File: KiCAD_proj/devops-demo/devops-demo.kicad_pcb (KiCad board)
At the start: 2 copper layers, 8 parts, among them J1 Conn_PinHeader_FTDI_1x06_P2.5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, SW1 SWITCH_JS102011JCQN, U1 ESP32-WROOM-32, U2 AMS1117-3.3

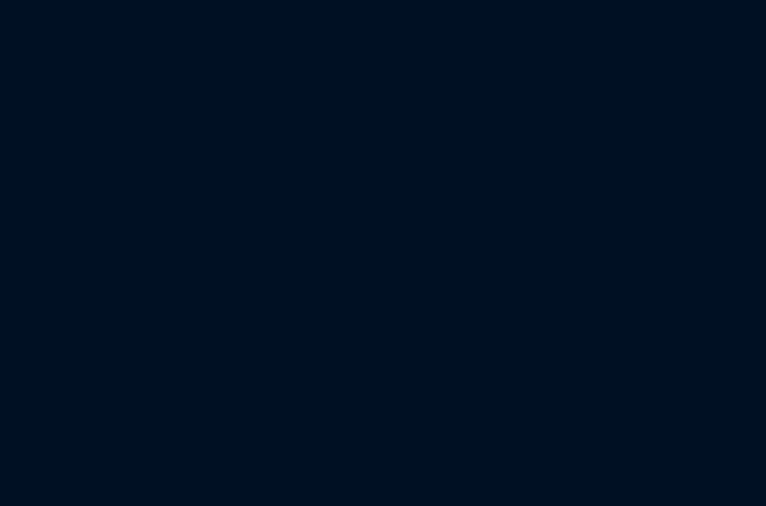
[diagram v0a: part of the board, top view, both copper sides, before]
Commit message: Added PWR and RESET circuits
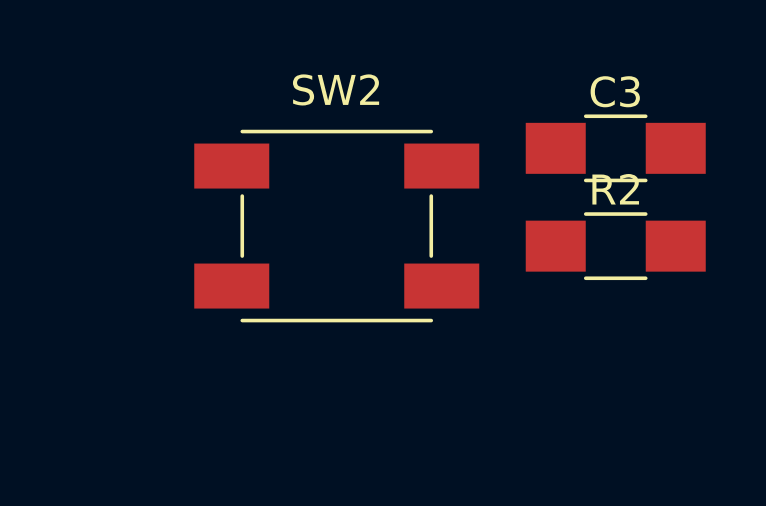
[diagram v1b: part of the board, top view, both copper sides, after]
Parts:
- added C3: 0.1uF, fab:C_1206, F.Cu at (211.2, 51.9)
- added R2: 10k, fab:R_1206, F.Cu at (211.2, 55.2)
- added SW2: BUTTON_B3SN, fab:Button_Omron_B3SN_6x6mm, F.Cu at (201.9, 54.5)
- C1: value C -> 10uF
- C2: value C -> 1uF
- R1: value R -> 100
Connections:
- U1 pad 1: Net-(U1-Pad1) -> GND
- U1 pad 15: Net-(U1-Pad1) -> GND
- U1 pad 3: Net-(U1-Pad3) -> EN
- U1 pad 38: Net-(U1-Pad1) -> GND
- U1 pad 39: Net-(U1-Pad1) -> GND

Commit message: Schema Captured
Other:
- net class Default: trace_width 0.25 -> 0.4
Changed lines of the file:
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@@
   )
   (page A4)
+  (title_block
+    (title "FA ESP32")
+    (date 2021-06-12)
+    (rev v01)
+    (company SahukarV)
+    (comment 2 https://creativecommons.org/licenses/by/4.0/)
+    (comment 3 "License: CC BY 4.0")
+    (comment 4 "Author: Manoj Sahukar")
+  )
   (layers
     (0 F.Cu signal)
@@
   )
   (setup
-    (last_trace_width 0.25)
+    (last_trace_width 0.4)
     (trace_clearance 0.2)
     (zone_clearance 0.508)
@@
   (net_class Default "This is the default net class."
     (clearance 0.2)
-    (trace_width 0.25)
+    (trace_width 0.4)
     (via_dia 0.8)
     (via_drill 0.4)

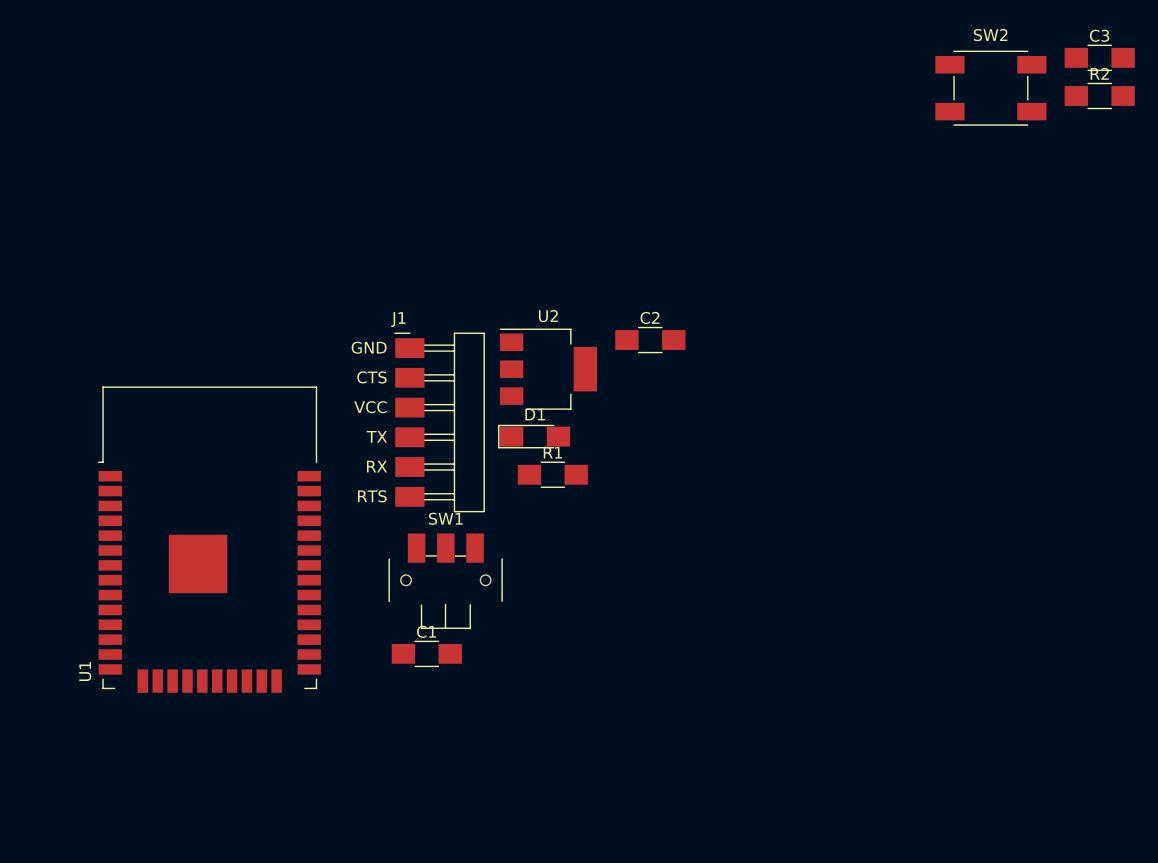
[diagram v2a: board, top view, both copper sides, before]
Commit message: Placed components and made corrections in schema
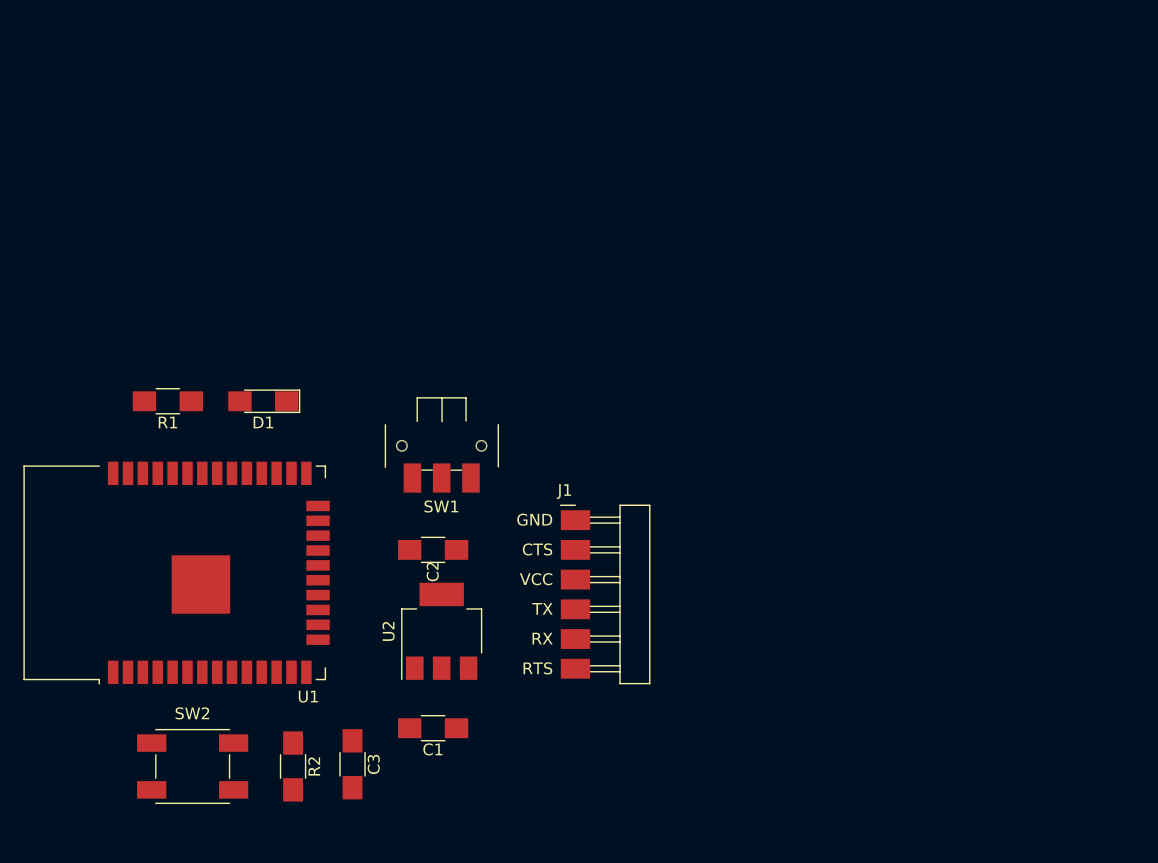
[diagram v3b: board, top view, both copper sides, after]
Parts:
- moved R2 89.6 mm to (142.2, 112.5), turned to 270 degrees
- moved SW2 89.5 mm to (133.7, 112.5)
- moved C3 87.9 mm to (147.3, 112.3), turned to 270 degrees
- moved R1 33.5 mm to (131.5, 81.3), turned to 180 degrees
- moved C2 25.8 mm to (154.2, 94.0), turned to 180 degrees
- moved U2 24.2 mm to (154.9, 100.9), turned to 90 degrees
- moved D1 23.4 mm to (139.7, 81.3), turned to 180 degrees
- moved J1 20.4 mm to (166.4, 91.4)
- moved SW1 11.5 mm to (154.9, 85.1), turned to 180 degrees
- moved C1 6.37 mm to (154.2, 109.2), turned to 180 degrees
- turned U1 to 90 degrees
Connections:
- C1 pad 1: +5V -> VCC
- D1 pad 1: +5V -> VCC
- J1 pad 1: Net-(J1-Pad1) -> GND
- J1 pad 3: Net-(J1-Pad3) -> VCC
- J1 pad 4: Net-(J1-Pad4) -> TXO
- J1 pad 5: Net-(J1-Pad5) -> RXI
- R2 pad 2: VDD -> +3V3
- SW1 pad 1: GND -> Net-(SW1-Pad1)
- SW1 pad 2: VDD -> GND
- SW1 pad 3: Power_+3V3 -> IO0
- U1 pad 2: VDD -> +3V3
- U1 pad 25: Net-(U1-Pad25) -> IO0
- U1 pad 34: Net-(U1-Pad34) -> TXO
- U1 pad 35: Net-(U1-Pad35) -> RXI
- U2 pad 1: Net-(U2-Pad1) -> GND
- U2 pad 3: +5V -> VCC

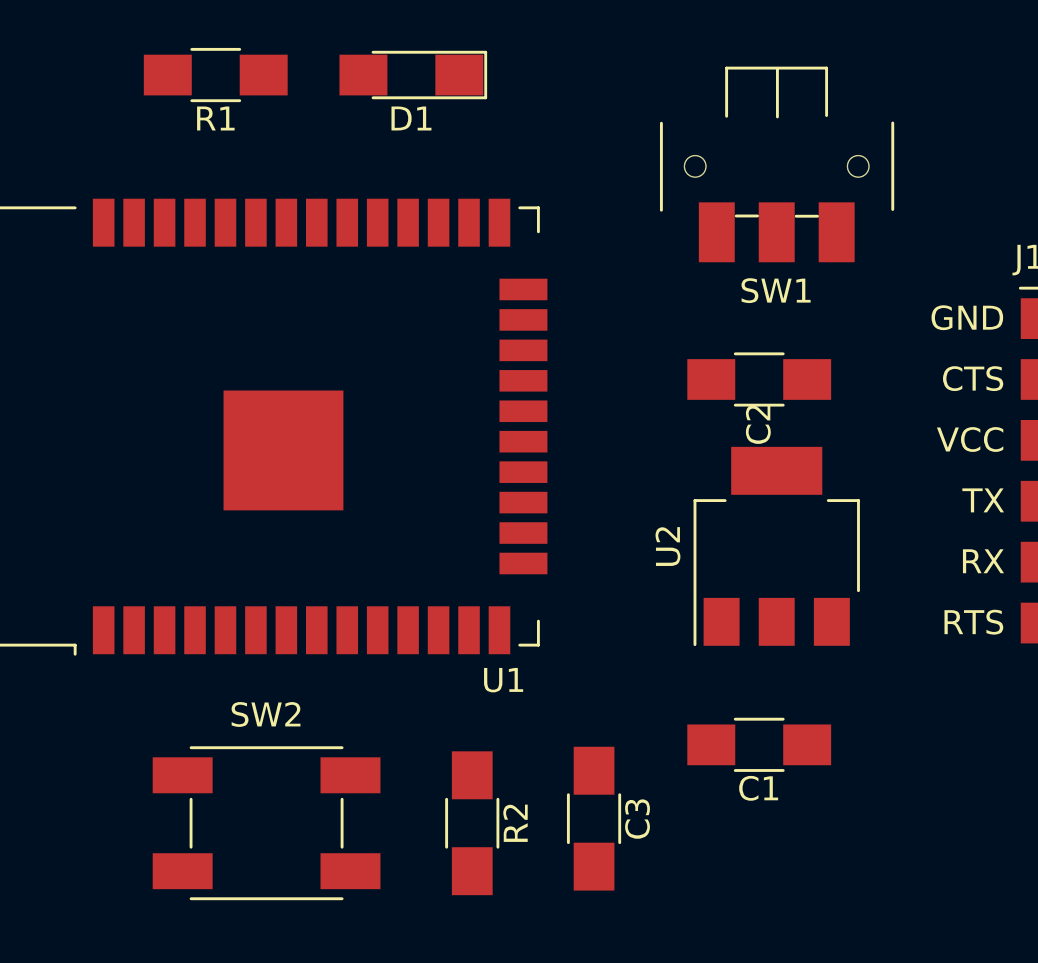
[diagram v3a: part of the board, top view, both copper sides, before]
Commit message: Added IO LED
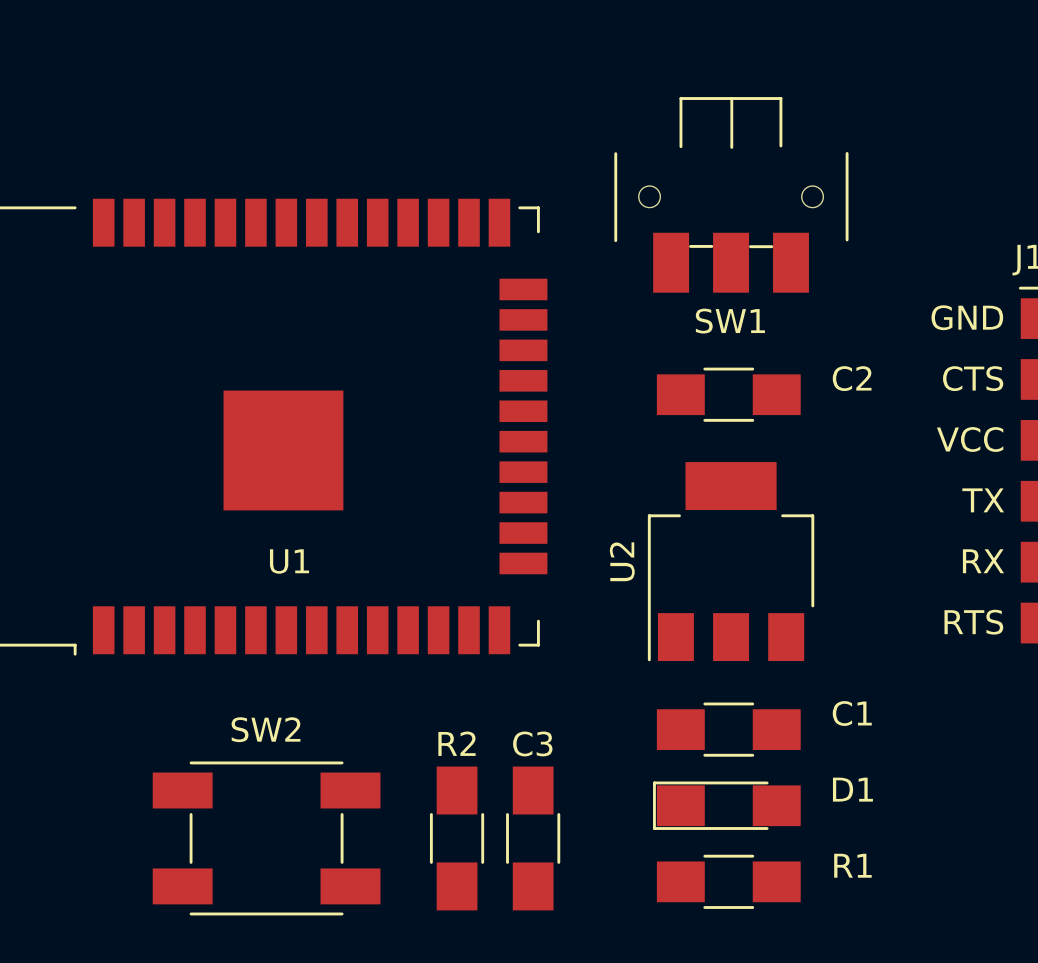
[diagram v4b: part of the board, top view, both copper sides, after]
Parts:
- moved R1 39.9 mm to (152.9, 114.9)
- moved D1 33.2 mm to (152.9, 111.8), turned to 0 degrees
- moved C3 2.67 mm to (144.8, 113.1)
- moved SW1 2.29 mm to (153.0, 86.4)
- moved U2 2.01 mm to (153.0, 101.6)
- moved C1 1.42 mm to (152.9, 108.6)
- moved C2 1.42 mm to (152.9, 94.6)
- moved R2 0.90 mm to (141.6, 113.1)
- moved SW2 0.64 mm to (133.7, 113.1)
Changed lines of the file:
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@@
   )
   (module fab:Button_Omron_B3SN_6x6mm (layer F.Cu)
-    (at 133.66 112.49)
+    (at 133.66 113.125)
     (descr "Surface Mount Tactile Switch for High-Density Packaging")
     (tags "Tactile Switch")
@@
   )
   (module fab:R_1206 (layer F.Cu)
-    (at 142.24 112.49 270)
+    (at 141.605 113.125 270)
     (descr "Resistor SMD 1206, hand soldering")
     (tags "resistor 1206")
     (attr smd)
-    (fp_text reference R2 (at 0 -1.85 90) (layer F.SilkS)
-      (effects (font (size 1 1) (thickness 0.15)))
-    )
-    (fp_text value 10k (at 0 1.9 90) (layer F.Fab)
+    (fp_text reference R2 (at -3.905 0 180) (layer F.SilkS)
+      (effects (font (size 1 1) (thickness 0.15)))
+    )
+    (fp_text value 10k (at 4.35 0 180) (layer F.Fab)
       (effects (font (size 1 1) (thickness 0.15)))
     )
@@
   )
   (module fab:C_1206 (layer F.Cu)
-    (at 147.32 112.3 270)
+    (at 144.78 113.125 270)
     (descr "Capacitor SMD 1206, hand soldering")
     (tags "capacitor 1206")
     (attr smd)
-    (fp_text reference C3 (at 0 -1.85 90) (layer F.SilkS)
-      (effects (font (size 1 1) (thickness 0.15)))
-    )
-    (fp_text value 0.1uF (at 0 1.9 90) (layer F.Fab)
+    (fp_text reference C3 (at -3.905 0 180) (layer F.SilkS)
+      (effects (font (size 1 1) (thickness 0.15)))
+    )
+    (fp_text value 0.1uF (at 4.35 -1.27 180) (layer F.Fab)
       (effects (font (size 1 1) (thickness 0.15)))
     )
@@
   )
   (module Package_TO_SOT_SMD:SOT-223-3_TabPin2 (layer F.Cu)
-    (at 154.94 100.94 90)
+    (at 153.035 101.575 90)
     (descr "module CMS SOT223 4 pins")
     (tags "CMS SOT")
@@
     (tags "Single 2.4 GHz Wi-Fi and Bluetooth combo  chip")
     (attr smd)
-    (fp_text reference U1 (at -10.61 8.43) (layer F.SilkS)
-      (effects (font (size 1 1) (thickness 0.15)))
-    )
-    (fp_text value ESP32-WROOM-32 (at 0 11.5 90) (layer F.Fab)
+    (fp_text reference U1 (at -5.66 -0.5) (layer F.SilkS)
+      (effects (font (size 1 1) (thickness 0.15)))
+    )
+    (fp_text value ESP32-WROOM-32 (at 4.5 -0.5 180) (layer F.Fab)
       (effects (font (size 1 1) (thickness 0.15)))
     )
@@
   )
   (module fab:Switch_SPDT_C&K_JS102011JCQN_9x3.6mm_P2.5mm (layer F.Cu)
-    (at 154.94 85.09 180)
+    (at 153.035 86.36 180)
     (descr http://www.ckswitches.com/media/1422/js.pdf)
     (tags "switch spdt")
@@
   )
   (module fab:R_1206 (layer F.Cu)
-    (at 131.54 81.28 180)
+    (at 152.94 114.935 180)
     (descr "Resistor SMD 1206, hand soldering")
     (tags "resistor 1206")
     (attr smd)
-    (fp_text reference R1 (at 0 -1.85) (layer F.SilkS)
-      (effects (font (size 1 1) (thickness 0.15)))
-    )
-    (fp_text value 100 (at 0 1.9) (layer F.Fab)
+    (fp_text reference R1 (at -5.175 0.635) (layer F.SilkS)
+      (effects (font (size 1 1) (thickness 0.15)))
+    )
+    (fp_text value 100 (at -5.175 -0.635) (layer F.Fab)
       (effects (font (size 1 1) (thickness 0.15)))
     )
@@
   )
   (module fab:LED_1206 (layer F.Cu)
-    (at 139.7 81.28 180)
+    (at 152.94 111.76)
     (descr "LED SMD 1206, hand soldering")
     (tags "LED 1206")
     (attr smd)
-    (fp_text reference D1 (at 0 -1.85) (layer F.SilkS)
-      (effects (font (size 1 1) (thickness 0.15)))
-    )
-    (fp_text value LED (at 0 1.9) (layer F.Fab)
+    (fp_text reference D1 (at 5.175 -0.635) (layer F.SilkS)
+      (effects (font (size 1 1) (thickness 0.15)))
+    )
+    (fp_text value LED (at 5.175 0.635) (layer F.Fab)
       (effects (font (size 1 1) (thickness 0.15)))
     )
@@
     (fp_line (start 3.25 1.1) (end 3.25 -1.11) (layer F.CrtYd) (width 0.05))
     (fp_line (start 3.25 1.1) (end -3.25 1.1) (layer F.CrtYd) (width 0.05))
-    (pad 1 smd rect (at -2 0 180) (size 2 1.7) (layers F.Cu F.Paste F.Mask)
+    (pad 1 smd rect (at -2 0) (size 2 1.7) (layers F.Cu F.Paste F.Mask)
       (net 37 VCC))
-    (pad 2 smd rect (at 2 0 180) (size 2 1.7) (layers F.Cu F.Paste F.Mask)
+    (pad 2 smd rect (at 2 0) (size 2 1.7) (layers F.Cu F.Paste F.Mask)
       (net 3 "Net-(D1-Pad2)"))
     (model ${KISYS3DMOD}/LEDs.3dshapes/LED_1206.wrl
@@
   )
   (module fab:C_1206 (layer F.Cu)
-    (at 154.21 93.98 180)
+    (at 152.94 94.615 180)
     (descr "Capacitor SMD 1206, hand soldering")
     (tags "capacitor 1206")
     (attr smd)
-    (fp_text reference C2 (at 0 -1.85 270) (layer F.SilkS)
-      (effects (font (size 1 1) (thickness 0.15)))
-    )
-    (fp_text value 1uF (at 0 1.9) (layer F.Fab)
+    (fp_text reference C2 (at -5.175 0.635) (layer F.SilkS)
+      (effects (font (size 1 1) (thickness 0.15)))
+    )
+    (fp_text value 1uF (at -5.175 -0.635) (layer F.Fab)
       (effects (font (size 1 1) (thickness 0.15)))
     )
@@
   )
   (module fab:C_1206 (layer F.Cu)
-    (at 154.21 109.22 180)
+    (at 152.94 108.585 180)
     (descr "Capacitor SMD 1206, hand soldering")
     (tags "capacitor 1206")
     (attr smd)
-    (fp_text reference C1 (at 0 -1.85) (layer F.SilkS)
-      (effects (font (size 1 1) (thickness 0.15)))
-    )
-    (fp_text value 10uF (at 0 1.9) (layer F.Fab)
-      (effects (font (size 1 1) (thickness 0.15)))
-    )
+    (fp_text reference C1 (at -5.175 0.635) (layer F.SilkS)
+      (effects (font (size 1 1) (thickness 0.15)))
+    )
+    (fp_text value 10uF (at -5.175 -0.635) (layer F.Fab)
+      (effects (font (size 1 1) (thickness 0.15)))
+    )

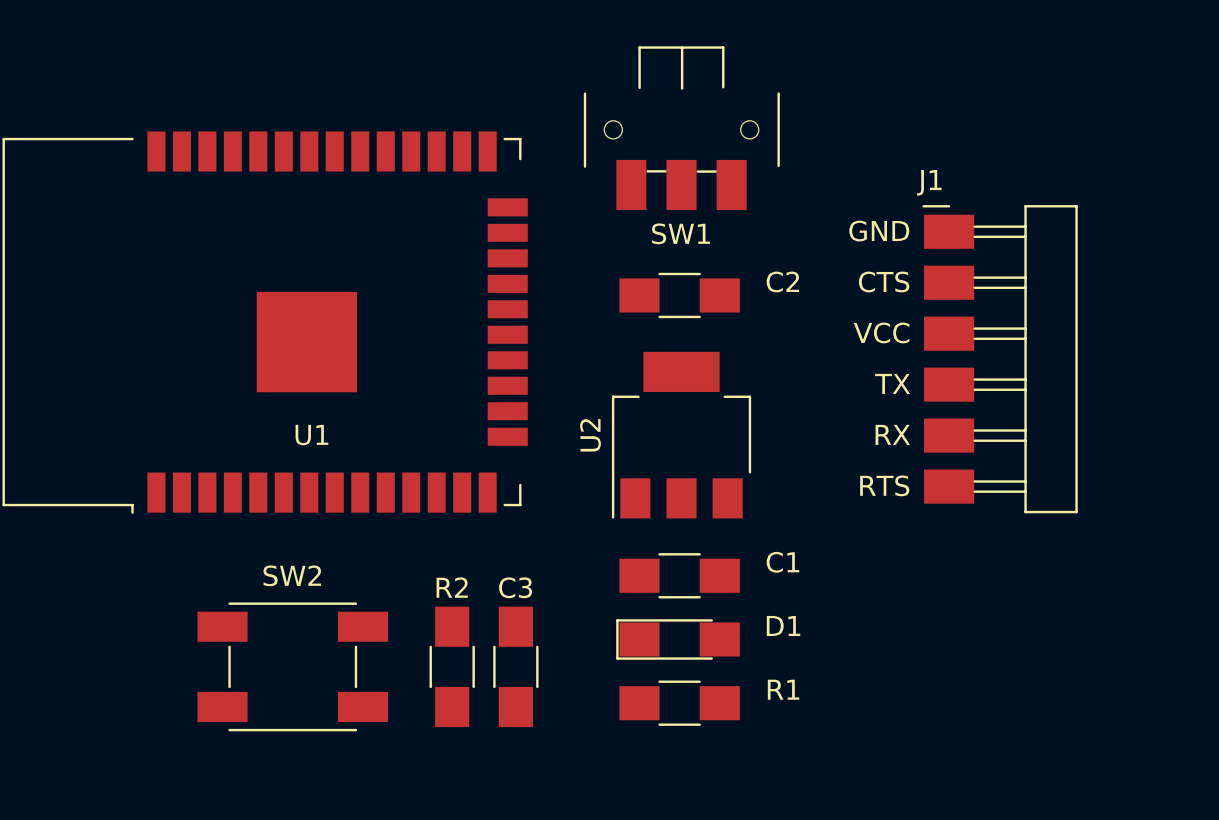
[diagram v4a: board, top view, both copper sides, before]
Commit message: Refine placement and draw outline
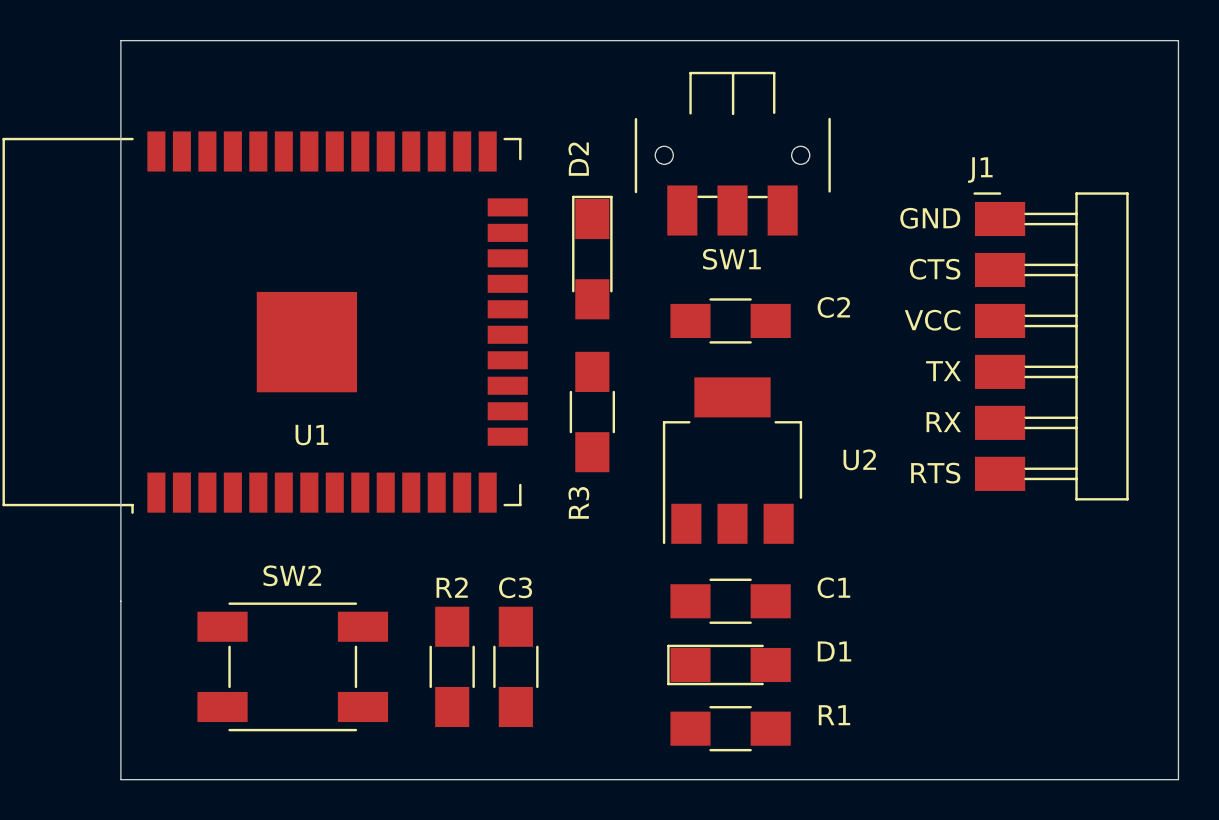
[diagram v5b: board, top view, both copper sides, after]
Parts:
- added D2: LED, fab:LED_1206, F.Cu at (148.6, 92.8)
- added R3: 100, fab:R_1206, F.Cu at (148.6, 100.4)
- moved C1 2.84 mm to (155.5, 109.9)
- moved C2 2.84 mm to (155.5, 95.9)
- moved D1 2.84 mm to (155.5, 113.0)
- moved R1 2.84 mm to (155.5, 116.2)
- moved SW1 2.84 mm to (155.6, 87.6)
- moved U2 2.84 mm to (155.6, 102.8)
- moved J1 2.62 mm to (168.9, 90.8)
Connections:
- U1 pad 24: Net-(U1-Pad24) -> IO2
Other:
- board outline added: 52.7 x 36.8 mm
